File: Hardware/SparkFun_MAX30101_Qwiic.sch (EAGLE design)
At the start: 33 parts, among them J1 PTH, J3 QWIIC_RA, J5 QWIIC_RA, Q6 20V/0.2A/8MHz/1.2Ω/1Vth, Q8 20V/0.2A/8MHz/1.2Ω/1Vth, U1 1.8V/100mA, U2 MAX30101

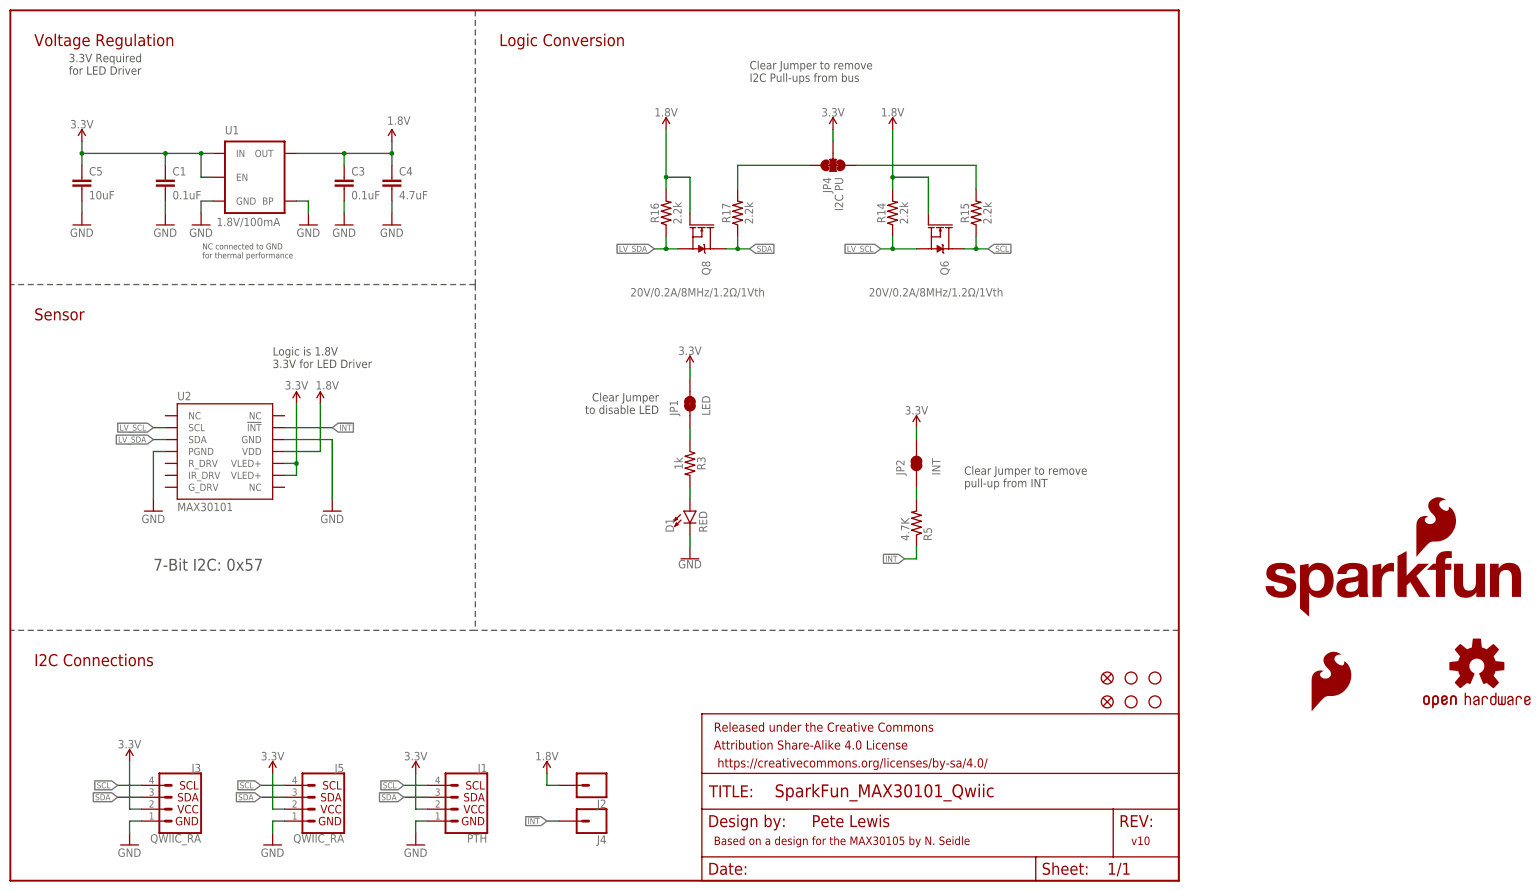
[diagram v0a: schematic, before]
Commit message: Qwiic logo in SCH and sch cleanup
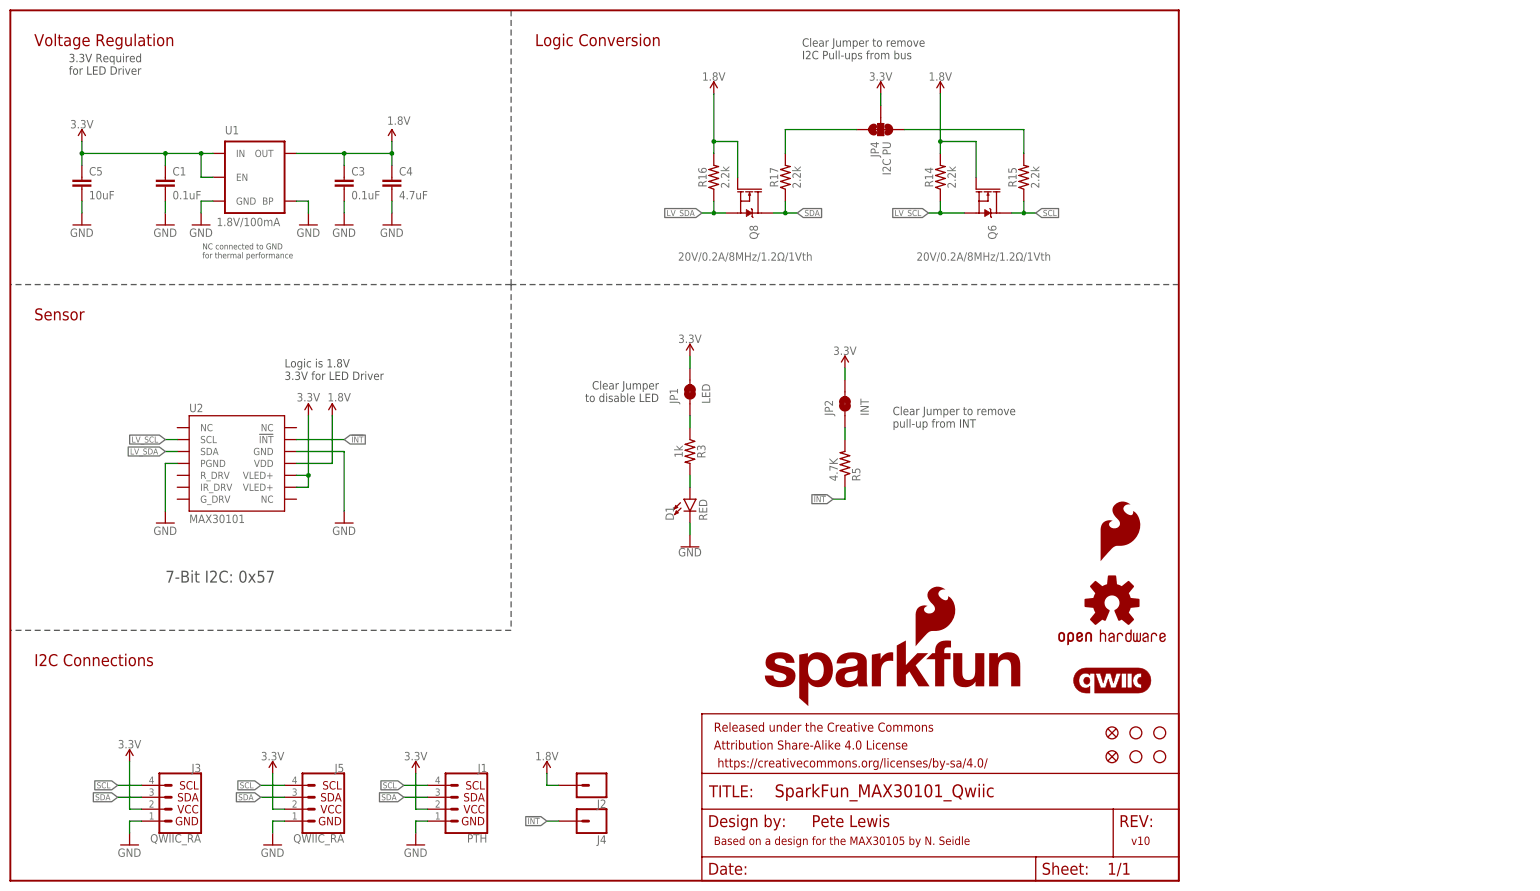
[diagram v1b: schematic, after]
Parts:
- added LOGO3: QWIIC_LOGO_5MM, SparkFun-Aesthetics:QWIIC_LOGO_5MM
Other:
- moved on the sheet: D1, JP1, JP2, JP4, Q6, Q8, R14, R15, R16, R17, R3, R5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

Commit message: Added 5V step up for green LED and review changes
-Added in 5V step up circuit to provide 5V for Green LED
-Add fids to bottom
-move power led label to text only
-3.3V trace could loose a via and then stitch up gnd with more vias
-move IC device to the true MAX30105 in the library.
-flip v10 in copper to read "along" the bottom.
-remove JP labels to jumpers, since they already have the names of their purposes.
-input voltage range in sch.
-Change 1.8V label flag to an output
-add typical current consuption for the sensor in the schematic near the IC symbol
-Move QWIIC lozenge to right over by the qwiic connector.
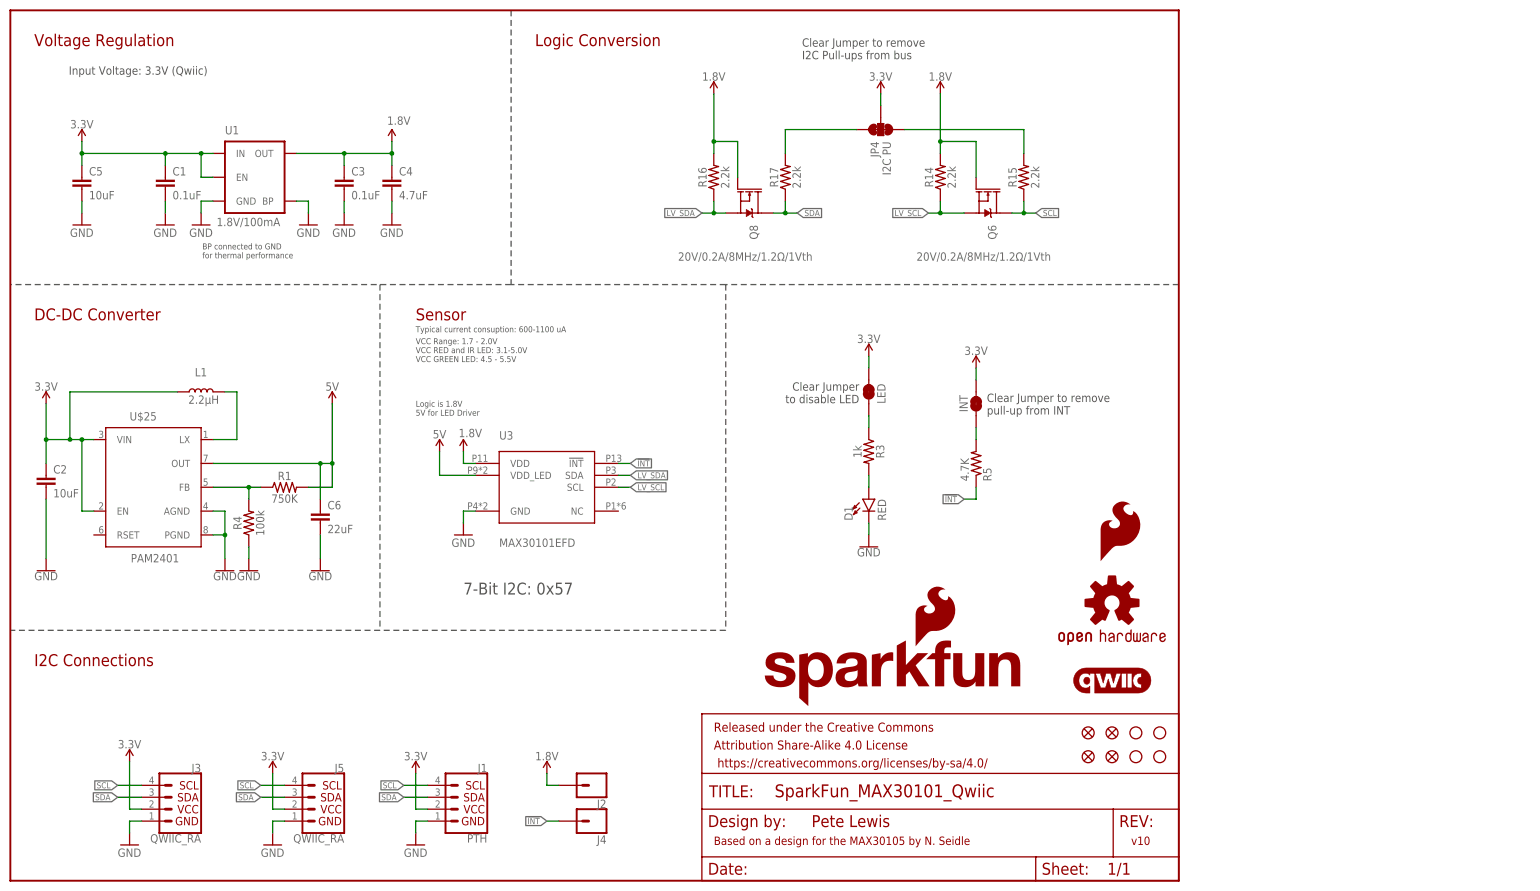
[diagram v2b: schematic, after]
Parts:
- removed U2: MAX30101, SparkFun-Sensors:MAX30105SMD
- added C2: 10uF, SparkFun-Capacitors:10UF-0603-6.3V-20%
- added C6: 22uF, SparkFun-Capacitors:22UF-0805-6.3V-20%
- added FID3, FID4: FIDUCIAL1X2, SparkFun-Aesthetics:FIDUCIAL1X2
- added L1: 2.2μH, SparkFun-Coils:2.2μH_SHIELDED_INDUCTOR
- added R1: 750K, SparkFun-Resistors:750KOHM-0603-1/10W-1%
- added R4: 100k, SparkFun-Resistors:100KOHM-0603-1/10W-1%
- added U$25: PAM2401, SparkFun-IC-Power:PAM2401
- added U3: MAX30101EFD, SparkFun-IC-Special-Function:MAX30101EFD
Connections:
- new net 5V: C6.1, R1.2, U$25.OUT, U3.VDD_LED
- new net N$2: R1.1, R4.2, U$25.FB
- new net N$3: L1.2, U$25.LX
- net !INT: now also U3.!INT; no longer U2.!INT
- net 1.8V: now also U3.VDD; no longer U2.VDD
- net 3.3V: now also C2.1, L1.1, U$25.EN, U$25.VIN; no longer U2.VLED+@10, U2.VLED+@9
- net GND: now also C2.2, C6.2, R4.1, U$25.AGND, U$25.PGND, U3.GND; no longer U2.GND, U2.PGND
- net LV_SCL: now also U3.SCL; no longer U2.SCL
- net LV_SDA: now also U3.SDA; no longer U2.SDA
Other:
- note added: "BP connected to GND for thermal performance"
- note added: "DC-DC Converter"
- note added: "Input Voltage: 3.3V (Qwiic)"
- note added: "Logic is 1.8V 5V for LED Driver"
- note added: "Typical current consuption: 600-1100 uA"
- note added: "VCC Range: 1.7 - 2.0V VCC RED and IR LED: 3.1-5.0V VCC GREEN LED: 4.5 - 5.5V"
- note removed: "3.3V Required for LED Driver"
- note removed: "Logic is 1.8V 3.3V for LED Driver"
- note removed: "NC connected to GND for thermal performance"
- moved on the sheet: D1, R3, R5

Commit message: design review #2 changes (post DC-DC converter addition)
-cleaned up sch around DC-DC converter
-added silk outline to MAX30101 IC
-replaced 4.7K resistor to updated package (without silk under it)
-updated Mosfets on logic level translation to latest library devices
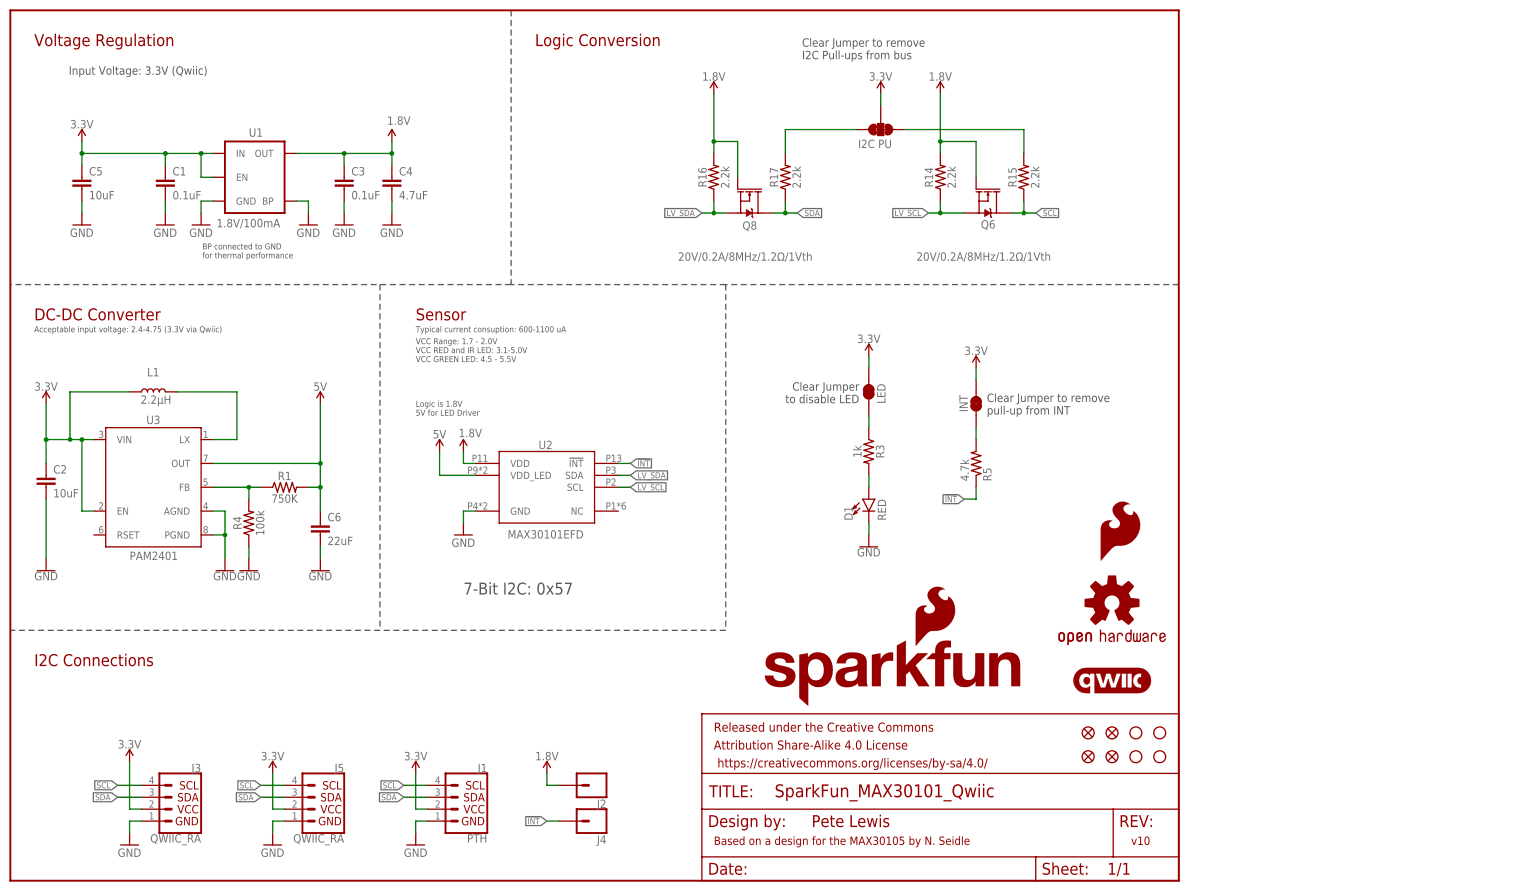
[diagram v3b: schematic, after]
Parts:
- removed U$25: PAM2401, SparkFun-IC-Power:PAM2401
- added U2: MAX30101EFD, SparkFun-IC-Special-Function:MAX30101EFD
- Q6, Q8: device SparkFun-DiscreteSemi:MOSFET-NCH-RE1C002UN -> SparkFun-DiscreteSemi:MOSFET-NCH-RE1C00UNTL
- R5: value 4.7K -> 4.7k; device SparkFun-Resistors:4.7KOHM-1/10W-1%(0603) -> SparkFun-Resistors:4.7KOHM-0603-1/10W-1%
- U3: value MAX30101EFD -> PAM2401; device SparkFun-IC-Special-Function:MAX30101EFD -> SparkFun-IC-Power:PAM2401
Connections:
- net !INT: now also U2.!INT; no longer U3.!INT
- net 1.8V: now also U2.VDD; no longer U3.VDD
- net 3.3V: now also U3.EN, U3.VIN; no longer U$25.EN, U$25.VIN
- net 5V: now also U2.VDD_LED, U3.OUT; no longer U$25.OUT, U3.VDD_LED
- net GND: now also U2.GND, U3.AGND, U3.PGND; no longer U$25.AGND, U$25.PGND, U3.GND
- net LV_SCL: now also U2.SCL; no longer U3.SCL
- net LV_SDA: now also U2.SDA; no longer U3.SDA
- net N$2: now also U3.FB; no longer U$25.FB
- net N$3: now also U3.LX; no longer U$25.LX
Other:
- note added: "Acceptable input voltage: 2.4-4.75 (3.3V via Qwiic)"
- moved on the sheet: C6, L1

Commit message: Added more bypass caps to 5V and 1.8V, bumped version to v11
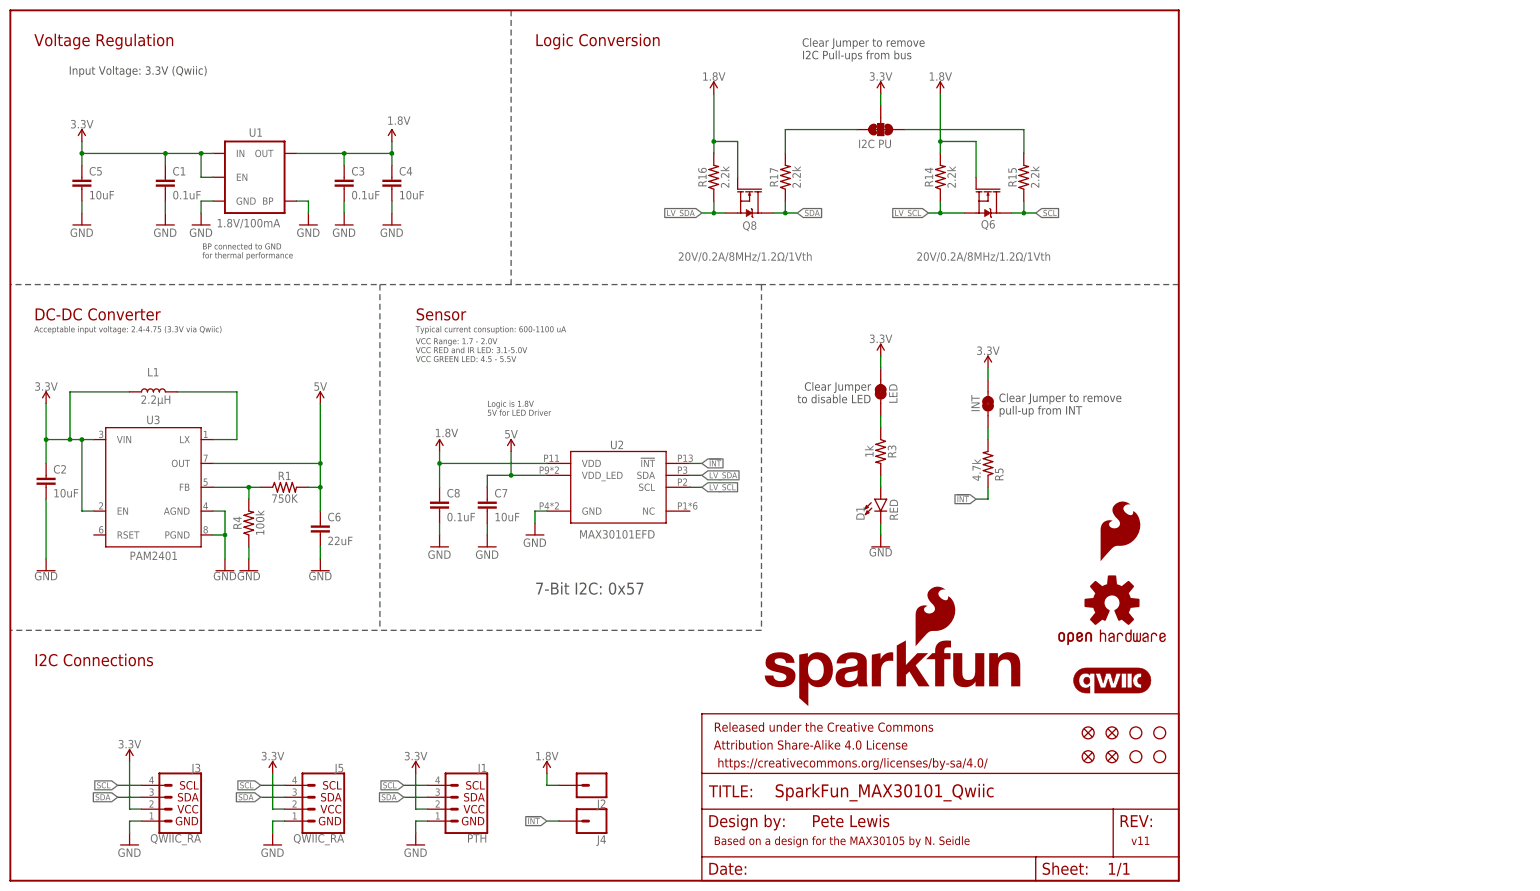
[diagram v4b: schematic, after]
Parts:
- added C7: 10uF, SparkFun-Capacitors:10UF-0603-6.3V-20%
- added C8: 0.1uF, SparkFun-Capacitors:0.1UF-0402-16V-10%
- C1, C3: device SparkFun-Capacitors:0.1UF-0603-25V-(+80/-20%) -> SparkFun-Capacitors:0.1UF-0402-16V-10%
- C4: value 4.7uF -> 10uF; device SparkFun-Capacitors:4.7UF-0603-6.3V-(10%) -> SparkFun-Capacitors:10UF-0603-6.3V-20%
- C5: device SparkFun-Capacitors:10UF-0805-10V-10% -> SparkFun-Capacitors:10UF-0603-6.3V-20%
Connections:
- net 1.8V: now also C8.1
- net 5V: now also C7.1
- net GND: now also C7.2, C8.2
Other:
- note added: "v11"
- note removed: "v10"
- moved on the sheet: D1, R3, R5, U2
